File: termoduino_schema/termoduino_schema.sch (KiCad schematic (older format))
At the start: 20 parts

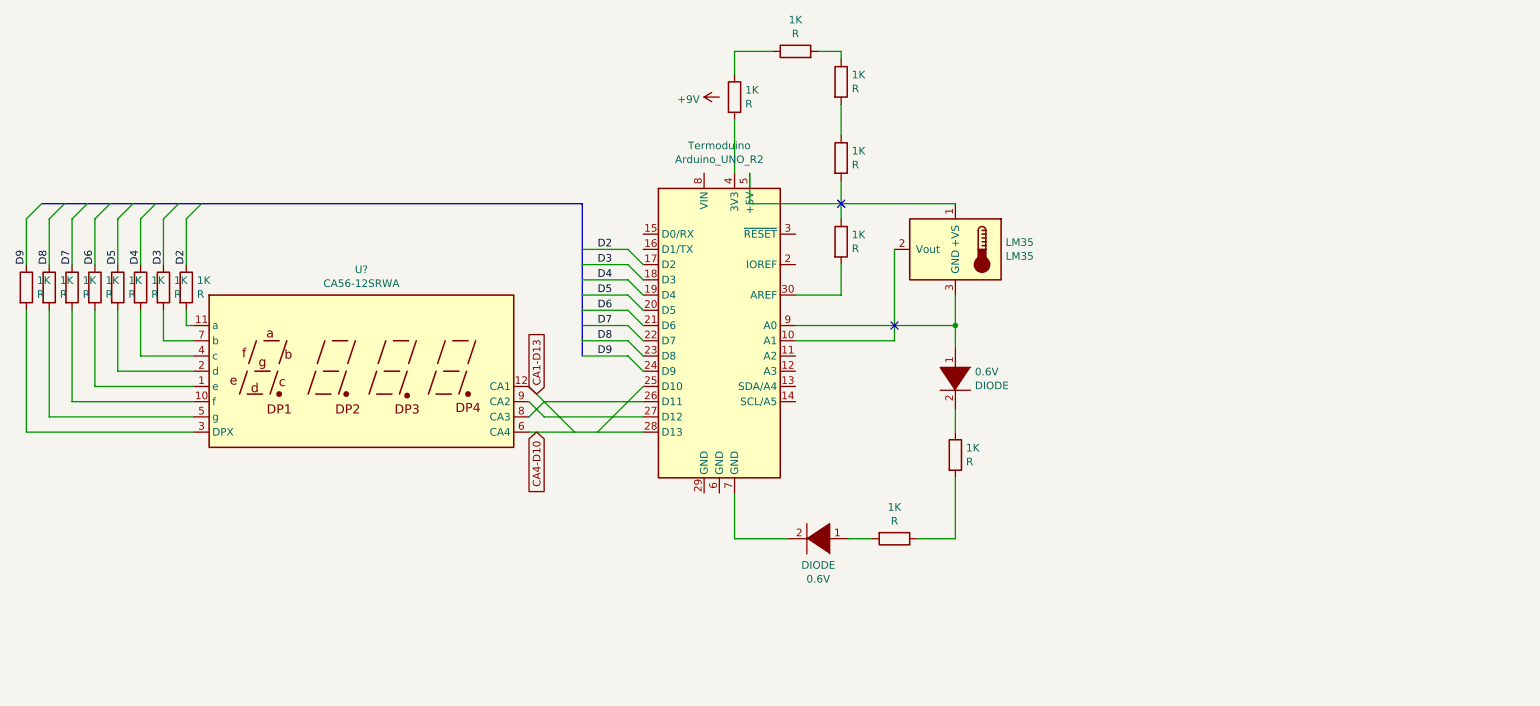
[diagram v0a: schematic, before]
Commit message: UPDATE: FIX power suppley schema
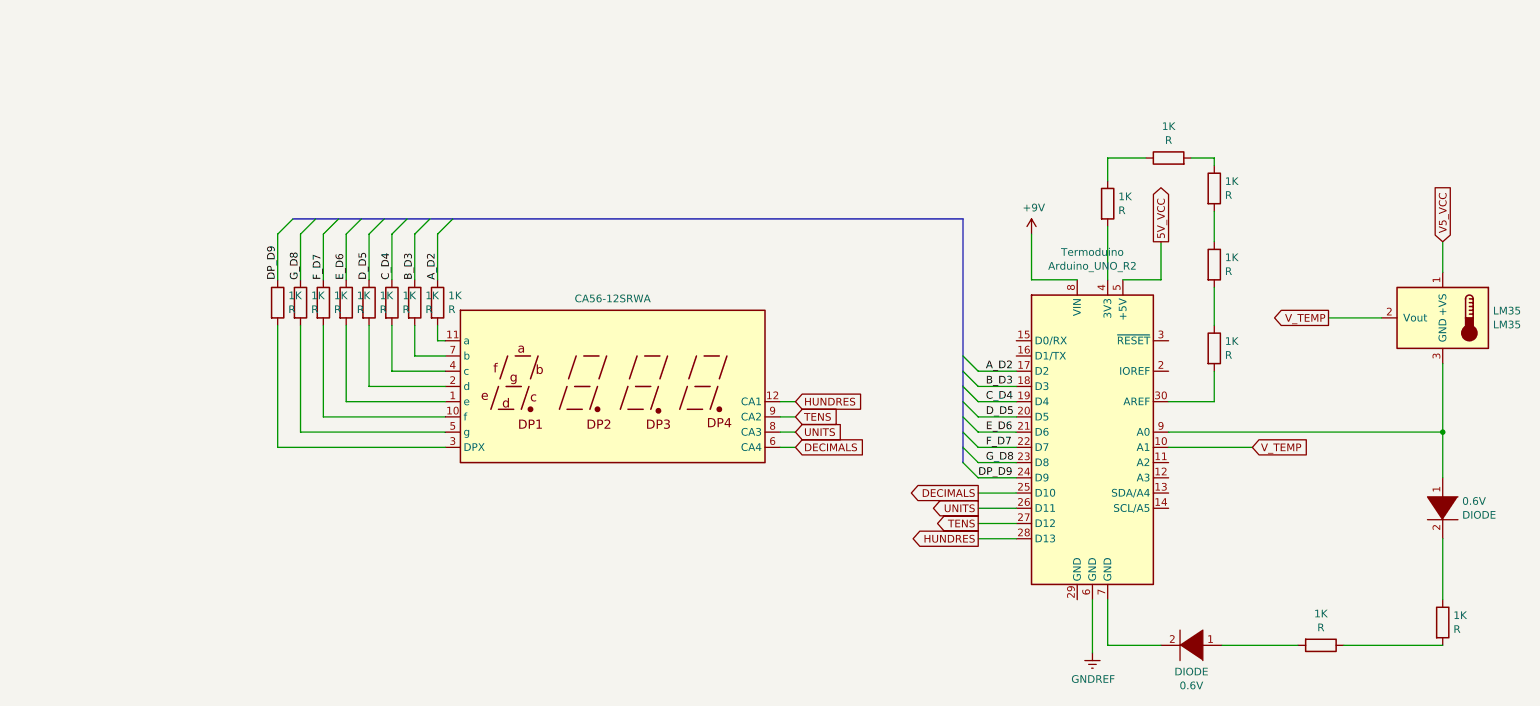
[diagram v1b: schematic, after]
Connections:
- net labels added: 5V_VCC, A_D2, B_D3, C_D4, DECIMALS, DP_D9, D_D5, E_D6, F_D7, GNDREF, G_D8, HUNDRES, TENS, UNITS, V5_VCC, V_TEMP
- net labels removed: CA1-D13, CA4-D10, D2, D3, D4, D5, D6, D7, D8, D9
- wire segments 57 -> 65
- no-connect marks 2 -> 0
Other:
- moved on the sheet: 0.6V, 1K, LM35, Termoduino
